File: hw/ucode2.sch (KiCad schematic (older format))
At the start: 16 parts, among them U801 74HC00, U802 74HC590, U803 27C64, U804 27C64, U805 27C64, U806 27C64, U807 74HCT175, U808 74HCT175, U809 74HCT175, U810 74HCT175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

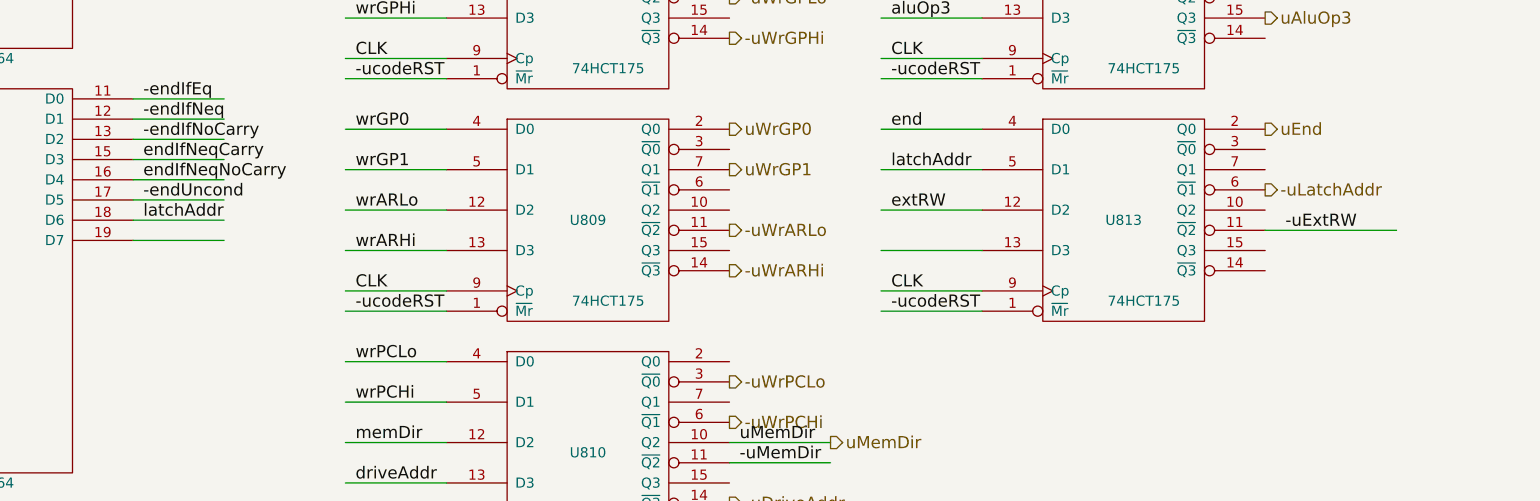
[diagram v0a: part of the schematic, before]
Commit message: add explicit signal to latch condition codes
Was able to use microcode bits more efficiently (to make
room for the new signal) by putting the combinational
logic to generate the external read/write signals after
the '175 microcode signal registers.  This should be fine
as long as memDir is set appropriately before the extRW
signal is asserted.  (No glitches should be possible.)
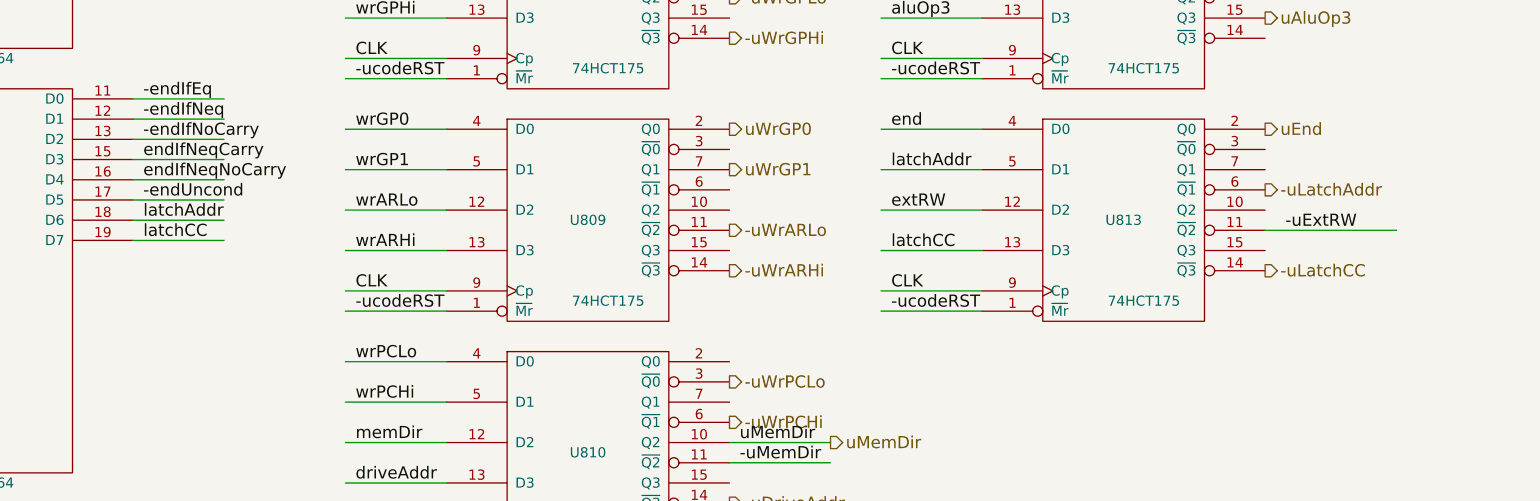
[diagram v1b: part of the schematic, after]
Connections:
- net labels added: -uLatchCC, latchCC
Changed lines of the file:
@@
 Text Label 11050 7950 0    60   ~ 0
 -uExtRW
+Text Label 5400 8000 0    60   ~ 0
+latchCC
+Text HLabel 10950 8150 2    60   Output ~ 0
+-uLatchCC
+Text Label 9100 8050 0    60   ~ 0
+latchCC
 $EndSCHEMATC

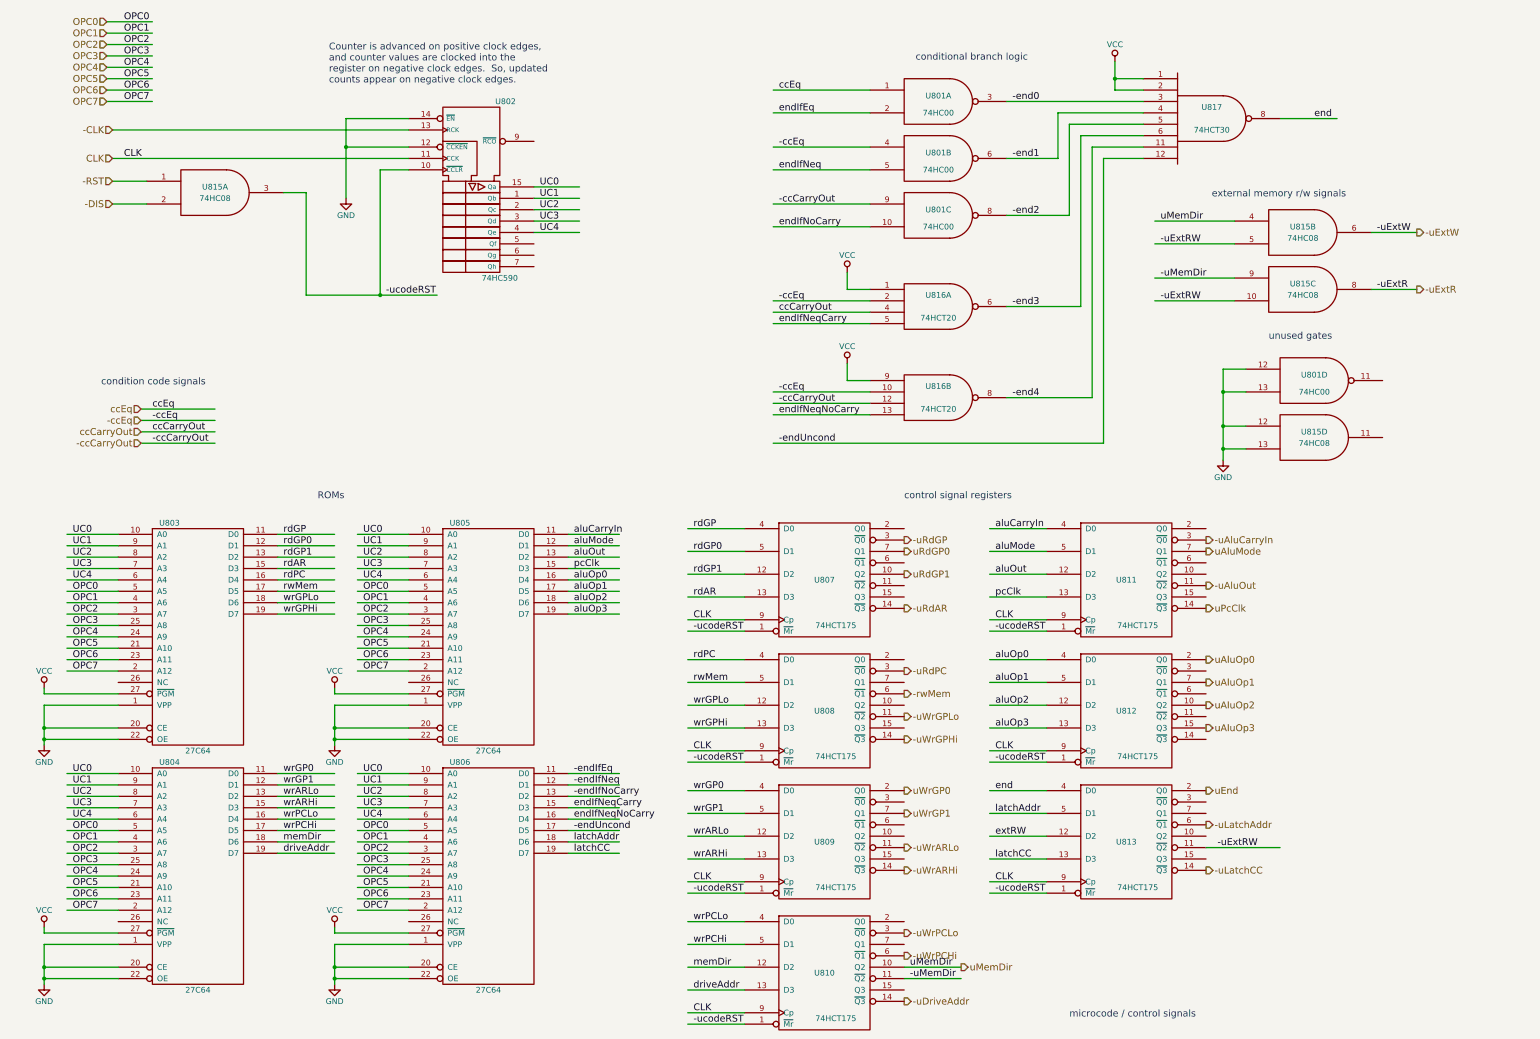
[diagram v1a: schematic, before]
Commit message: remove AR registers, switch to new ucode impl
Note that there is a bug in the ucode module:
the -uExtW and -uExtR signals are generated incorrectly.
(They need to be OR gates, not AND gates, so that
they can be held high when -uExtRW is not asserted.)
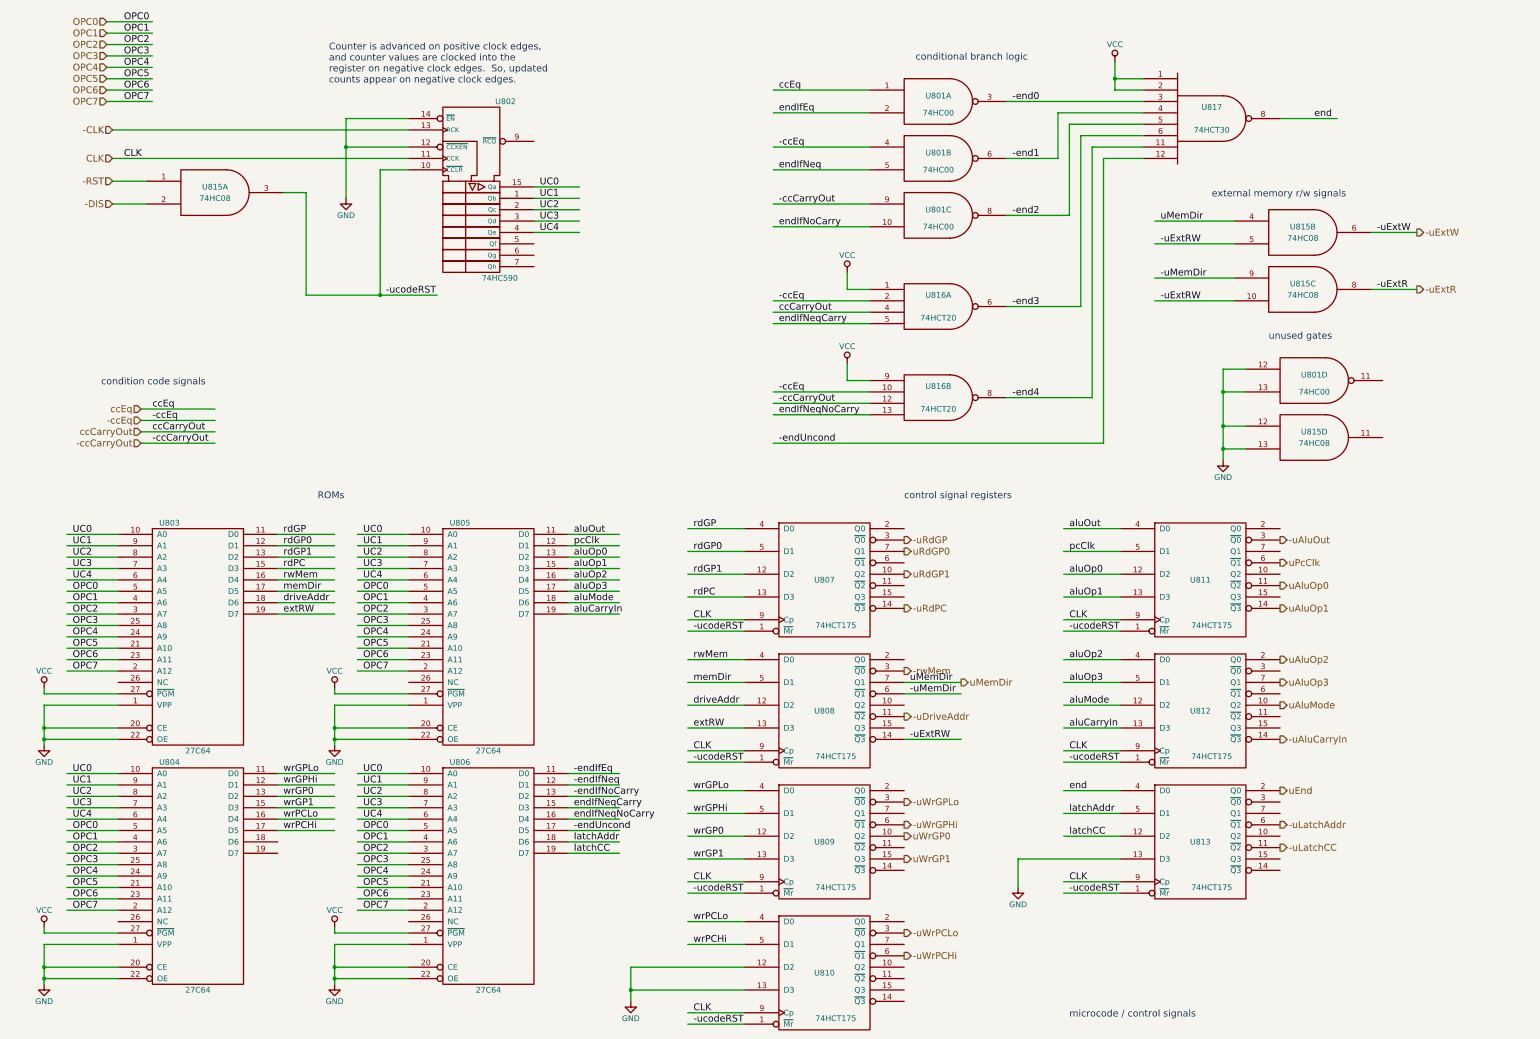
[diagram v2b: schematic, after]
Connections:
- net labels removed: -uRdAR, -uWrARHi, -uWrARLo, rdAR, wrARHi, wrARLo
- wire segments 243 -> 236
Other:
- moved on the sheet: U811, U812, U813

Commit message: fix logic generating -uExtW/-uExtR signals
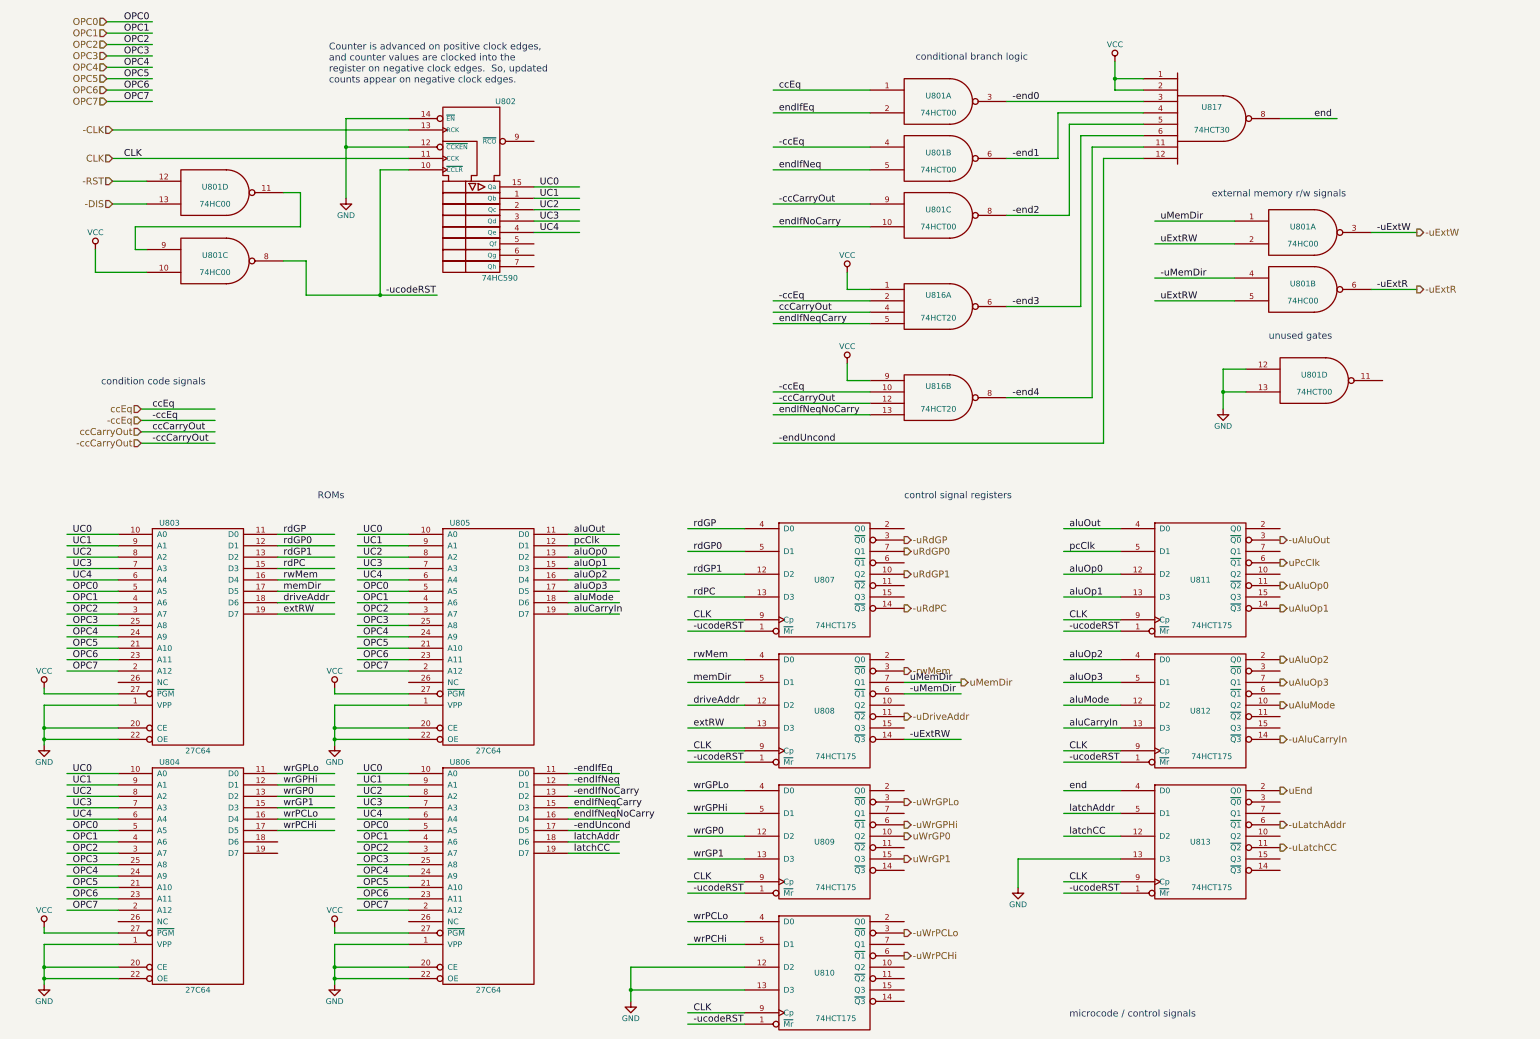
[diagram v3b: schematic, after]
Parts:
- removed U815: 74HC08, symbol 74LS08
- added U801: 74HC00, symbol 74LS00
- U801: value 74HC00 -> 74HCT00
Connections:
- net labels added: uExtRW
- wire segments 236 -> 241

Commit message: account for opfetch for -uExtR and -uRwMem
-uExtR should be asserted whenever -opReadMem is asserted,
and -uRwMem should be asserted whenever -opfetch is asserted.

Did this without additional chips, at the cost of requiring
74HCT10 rather than 74HCT20 in the conditional branch logic.
(Will have to buy these, but I've seen them on ebay.)

Also renumbered some of the chips in the ucode2 module
so that the numbering reflects the actual number of chips
(16).

Will need to carefully double check this to make sure it's
correct.
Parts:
- removed U801: 74HC00, symbol 74LS00
- removed U816: 74HCT20, symbol 74LS20
- added U814: 74HCT10, symbol 74LS10
- added U816: 74HC08, symbol 74LS08
- renumbered U817 to U815
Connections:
- net labels added: -opReadMem, -opfetch, -uRwMem
- net labels removed: -rwMem
- wire segments 241 -> 254
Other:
- note added: "Note that uMemDir is guaranteed\nto be correct when -opfetch is asserted,\nbecause the ucode unit is under reset\nand thus uMemdir is 0 (read)."
- moved on the sheet: U801A, U801B, U801C, U801D, U802, U815

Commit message: add missing signals to/from ucode2 module
Also, use a custom page size for the top-level
schematic.
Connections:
- wire segments 254 -> 241
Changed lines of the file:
@@
 	1250 2300 950  2300
 Wire Wire Line
-	2650 3100 3300 3100
-Wire Wire Line
-	3300 3100 3800 3100
+	2650 3100 3800 3100
 Wire Wire Line
 	3550 1650 950  1650
@@
 	3550 1800 3000 1800
 Wire Wire Line
-	3000 1550 3000 1800
-Wire Wire Line
-	3000 1800 3000 2250
+	3000 1550 3000 2250
 Wire Wire Line
 	3550 1550 3000 1550
@@
 	1400 6700 750  6700
 Wire Wire Line
-	750  6700 750  6900
-Wire Wire Line
-	750  6900 750  7000
-Wire Wire Line
-	750  7000 750  7050
+	750  6700 750  7050
 Wire Wire Line
 	1400 6900 750  6900
@@
 	3950 6700 3300 6700
 Wire Wire Line
-	3300 6700 3300 6900
-Wire Wire Line
-	3300 6900 3300 7000
-Wire Wire Line
-	3300 7000 3300 7050
+	3300 6700 3300 7050
 Wire Wire Line
 	3950 6900 3300 6900
@@
 	1400 8800 750  8800
 Wire Wire Line
-	750  8800 750  9000
-Wire Wire Line
-	750  9000 750  9100
-Wire Wire Line
-	750  9100 750  9150
+	750  8800 750  9150
 Wire Wire Line
 	1400 9000 750  9000
@@
 	3950 8800 3300 8800
 Wire Wire Line
-	3300 8800 3300 9000
-Wire Wire Line
-	3300 9000 3300 9100
-Wire Wire Line
-	3300 9100 3300 9150
+	3300 8800 3300 9150
 Wire Wire Line
 	3950 9000 3300 9000
@@
 	8500 1300 8750 1300
 Wire Wire Line
-	8500 1050 8500 1200
-Wire Wire Line
-	8500 1200 8500 1300
+	8500 1050 8500 1300
 Wire Wire Line
 	8750 1200 8500 1200
@@
 	12650 1650 13050 1650
 Wire Wire Line
-	11250 4050 11250 4250
-Wire Wire Line
-	11250 4250 11250 4400
+	11250 4050 11250 4400
 Wire Wire Line
 	8300 6500 8800 6500
@@
 	6900 9000 5900 9000
 Wire Wire Line
-	5900 9000 5900 9200
-Wire Wire Line
-	5900 9200 5900 9300
+	5900 9000 5900 9300
 Wire Wire Line
 	6900 9200 5900 9200

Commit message: allow -opfetch to drive address to addr bus
This is necessary during opfetch, when the microcode
module does not assert -uDriveAddr on its own.
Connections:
- wire segments 241 -> 255
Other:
- note removed: "unused gates"
- moved on the sheet: U816D
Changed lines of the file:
@@
 Text Label 6450 6700 0    60   ~ 0
 driveAddr
-Text HLabel 8300 6800 2    60   Output ~ 0
+Text HLabel 13050 3350 2    60   Output ~ 0
 -uDriveAddr
 Text Label 5400 7300 0    60   ~ 0
@@
 Text HLabel 11600 7750 2    60   Output ~ 0
 -uLatchAddr
-Text Notes 11750 3900 0    60   ~ 0
-unused gates
-$Comp
-L GND #PWR?
-U 1 1 59522CEA
-P 11250 4400
-F 0 "#PWR?" H 11250 4150 50  0001 C CNN
-F 1 "GND" H 11250 4250 50  0000 C CNN
-F 2 "" H 11250 4400 50  0001 C CNN
-F 3 "" H 11250 4400 50  0001 C CNN
-	1    11250 4400
-	1    0    0    -1
-$EndComp
 $Comp
 L 74LS00 U801
@@
 Text Label 8350 6400 0    60   ~ 0
 -uRwMem
-Text HLabel 10750 2750 0    60   Input ~ 0
+Text HLabel 9950 2750 0    60   Input ~ 0
 -opfetch
 Text Label 10800 2950 0    60   ~ 0
@@
 L 74LS08 U816
 U 4 1 59866B3C
-P 12050 4150
-F 0 "U816" H 12050 4200 50  0000 C CNN
-F 1 "74HC08" H 12050 4100 50  0000 C CNN
-F 2 "" H 12050 4150 50  0001 C CNN
-F 3 "" H 12050 4150 50  0001 C CNN
-	4    12050 4150
+P 12050 3350
+F 0 "U816" H 12050 3400 50  0000 C CNN
+F 1 "74HC08" H 12050 3300 50  0000 C CNN
+F 2 "" H 12050 3350 50  0001 C CNN
+F 3 "" H 12050 3350 50  0001 C CNN
+	4    12050 3350
 	1    0    0    -1
 $EndComp
@@
 	1250 2300 950  2300
 Wire Wire Line
-	2650 3100 3800 3100
+	2650 3100 3300 3100
+Wire Wire Line
+	3300 3100 3800 3100
 Wire Wire Line
 	3550 1650 950  1650
@@
 	3550 1800 3000 1800
 Wire Wire Line
-	3000 1550 3000 2250
+	3000 1550 3000 1800
+Wire Wire Line
+	3000 1800 3000 2250
 Wire Wire Line
 	3550 1550 3000 1550
@@
 	1400 6700 750  6700
 Wire Wire Line
-	750  6700 750  7050
+	750  6700 750  6900
+Wire Wire Line
+	750  6900 750  7000
+Wire Wire Line
+	750  7000 750  7050
 Wire Wire Line
 	1400 6900 750  6900
@@
 	3950 6700 3300 6700
 Wire Wire Line
-	3300 6700 3300 7050
+	3300 6700 3300 6900
+Wire Wire Line
+	3300 6900 3300 7000
+Wire Wire Line
+	3300 7000 3300 7050
 Wire Wire Line
 	3950 6900 3300 6900
@@
 	1400 8800 750  8800
 Wire Wire Line
-	750  8800 750  9150
+	750  8800 750  9000
+Wire Wire Line
+	750  9000 750  9100
+Wire Wire Line
+	750  9100 750  9150
 Wire Wire Line
 	1400 9000 750  9000
@@
 	3950 8800 3300 8800
 Wire Wire Line
-	3300 8800 3300 9150
+	3300 8800 3300 9000
+Wire Wire Line
+	3300 9000 3300 9100
+Wire Wire Line
+	3300 9100 3300 9150
 Wire Wire Line
 	3950 9000 3300 9000
@@
 	8300 6400 8800 6400
 Wire Wire Line
-	8300 6800 8300 6800
-Wire Wire Line
 	8300 8700 8300 8700
 Wire Wire Line
@@
 	8500 1300 8750 1300
 Wire Wire Line
-	8500 1050 8500 1300
+	8500 1050 8500 1200
+Wire Wire Line
+	8500 1200 8500 1300
 Wire Wire Line
 	8750 1200 8500 1200
@@
 	12650 1650 13050 1650
 Wire Wire Line
-	11250 4050 11250 4400
-Wire Wire Line
 	8300 6500 8800 6500
 Wire Wire Line
 	11450 1550 10750 1550
 Wire Wire Line
-	11450 4050 11250 4050
-Wire Wire Line
-	11450 4250 11250 4250
-Connection ~ 11250 4250
-Wire Wire Line
 	2800 5900 3300 5900
 Wire Wire Line
@@
 	6900 9000 5900 9000
 Wire Wire Line
-	5900 9000 5900 9300
+	5900 9000 5900 9200
+Wire Wire Line
+	5900 9200 5900 9300
 Wire Wire Line
 	6900 9200 5900 9200
@@
 	12650 2250 13050 2250
 Wire Wire Line
-	11450 2750 10750 2750
+	11450 2750 10400 2750
+Wire Wire Line
+	10400 2750 9950 2750
 Wire Wire Line
 	11450 2950 10750 2950
 Wire Wire Line
 	12650 2850 13050 2850
-Text Notes 11250 3500 0    60   ~ 0
+Text Notes 11200 4000 0    60   ~ 0
 Note that uMemDir is guaranteed\nto be correct when -opfetch is asserted,\nbecause the ucode unit is under reset\nand thus uMemdir is 0 (read).
 Wire Wire Line
@@
 	1    0    0    -1
 $EndComp
+Wire Wire Line
+	11450 3250 10400 3250
+Wire Wire Line
+	10400 3250 10400 2750
+Connection ~ 10400 2750
+Wire Wire Line
+	11450 3450 10750 3450
+Wire Wire Line
+	12650 3350 13050 3350
+Wire Wire Line
+	8300 6800 8800 6800
+Text Label 8350 6800 0    60   ~ 0
+-uDriveAddr
+Text Label 10800 3450 0    60   ~ 0
+-uDriveAddr
 $EndSCHEMATC

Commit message: allow ALU output to be latched
We can do this with essentially no increase in
complexity, using a '573 latch rather than a '541
buffer for the ALU output.  I'm guessing this
might be useful for some instructions (to hold the
ALU output constant when its inputs might be
changing.)
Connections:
- net labels added: -uLatchALU, latchALU
